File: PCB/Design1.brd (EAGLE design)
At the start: 70 x 42 mm, 34 parts, among them J1 FTDI_DEVICE, U1 ATMEGA2560AU

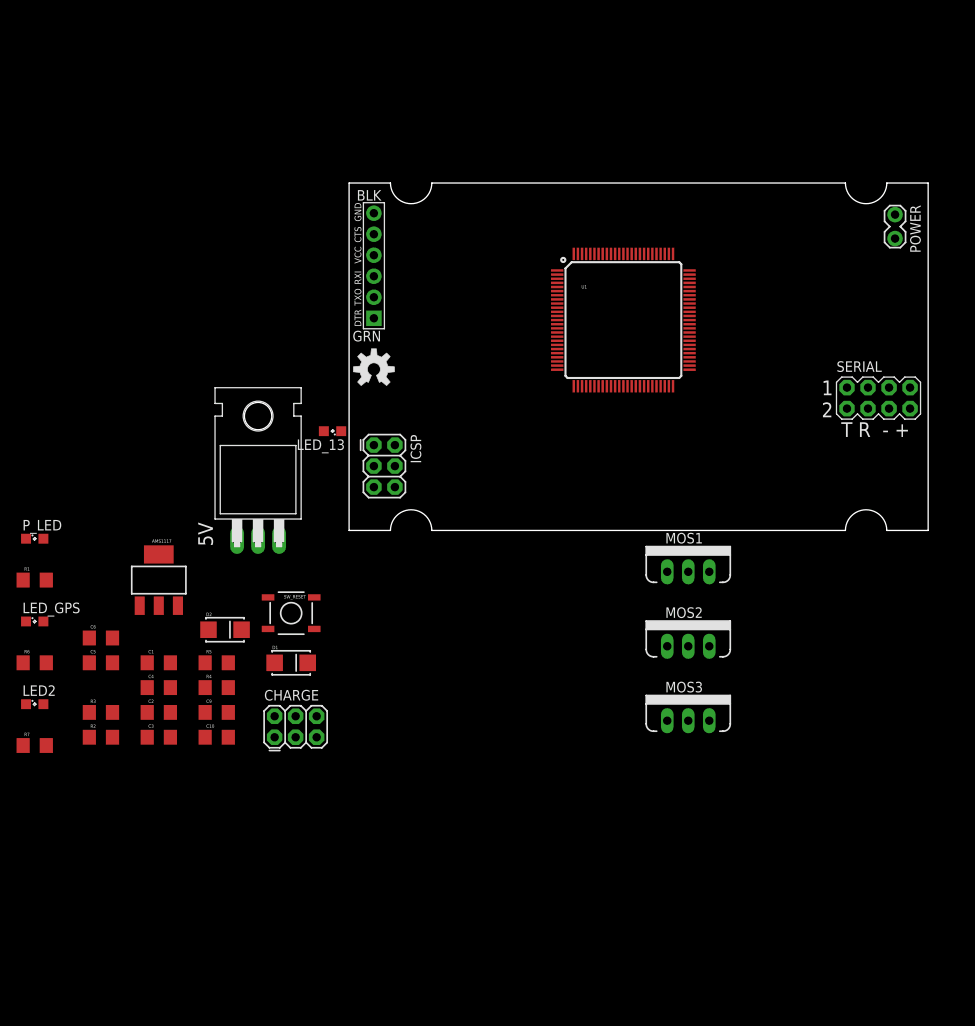
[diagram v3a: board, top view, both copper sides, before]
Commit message: Place mosfets
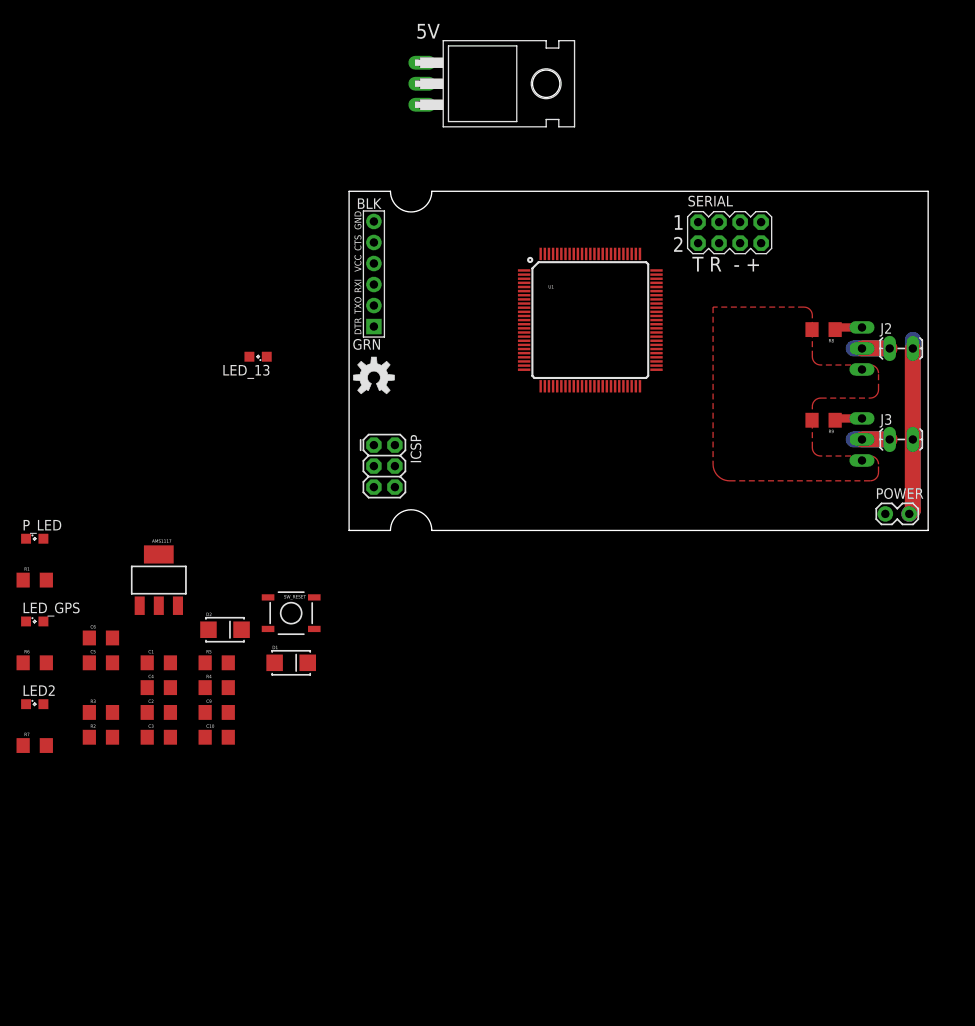
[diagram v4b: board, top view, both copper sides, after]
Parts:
- removed CHARGE: (no value), SparkFun-Connectors:2X3
- removed MOS3: (no value), SparkFun-DiscreteSemi:TO220V
- added J2, J3: (no value), SparkFun-Connectors:1X02_LOCK_LONGPADS
- added R8, R9: 10KΩ, SparkFun-Resistors:1206
- moved 5V 54.1 mm to (19.0, 54.0), turned to 270 degrees
- moved POWER 36.0 mm to (65.0, 2.00), turned to 0 degrees
- moved MOS1 34.2 mm to (62.0, 22.0), flipped to the bottom, turned to 270 degrees
- moved MOS2 32.6 mm to (62.0, 11.0), flipped to the bottom, turned to 270 degrees
- moved SERIAL 26.9 mm to (46.0, 36.0)
- moved LED_13 12.7 mm to (-11.0, 21.0)
- moved U1 4.00 mm to (29.2, 25.4)
- moved J1 1.00 mm to (3.00, 31.0)
- moved LOGO1 1.00 mm to (3.00, 18.5)
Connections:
- removed net CHARGE3: CHARGE.5
- removed net RAW: D2.A, POWER.2
- new net MOS1: J2.1, MOS1.2
- new net MOS2: J3.1, MOS2.2
- new net N$8: 5V.1, C1.1, C2.1, D2.C, R4.1
- net CHARGE1: now also MOS1.1, R8.1; no longer CHARGE.1
- net CHARGE2: now also MOS2.1, R9.1; no longer CHARGE.3
- net GND: now also R8.2, R9.2; no longer CHARGE.2, CHARGE.4, CHARGE.6, MOS3.3
- net VIN: now also D2.A, J2.2, J3.2, POWER.2; no longer 5V.1, C1.1, C2.1, D2.C, R4.1
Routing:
- net VIN: track 0.00 -> 41.4 mm
- net N$6: track 0.00 -> 4.00 mm
- net N$5: track 0.00 -> 4.00 mm
- net MOS2: track 0.00 -> 3.35 mm
- net MOS1: track 0.00 -> 3.35 mm
- net CHARGE1: track 0.00 -> 3.35 mm
- net CHARGE2: track 0.00 -> 3.33 mm
- added copper zone on layer 1, net GND
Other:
- board size 70 x 42 mm -> 70 x 41 mm

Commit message: switch to SMT 5v regulators
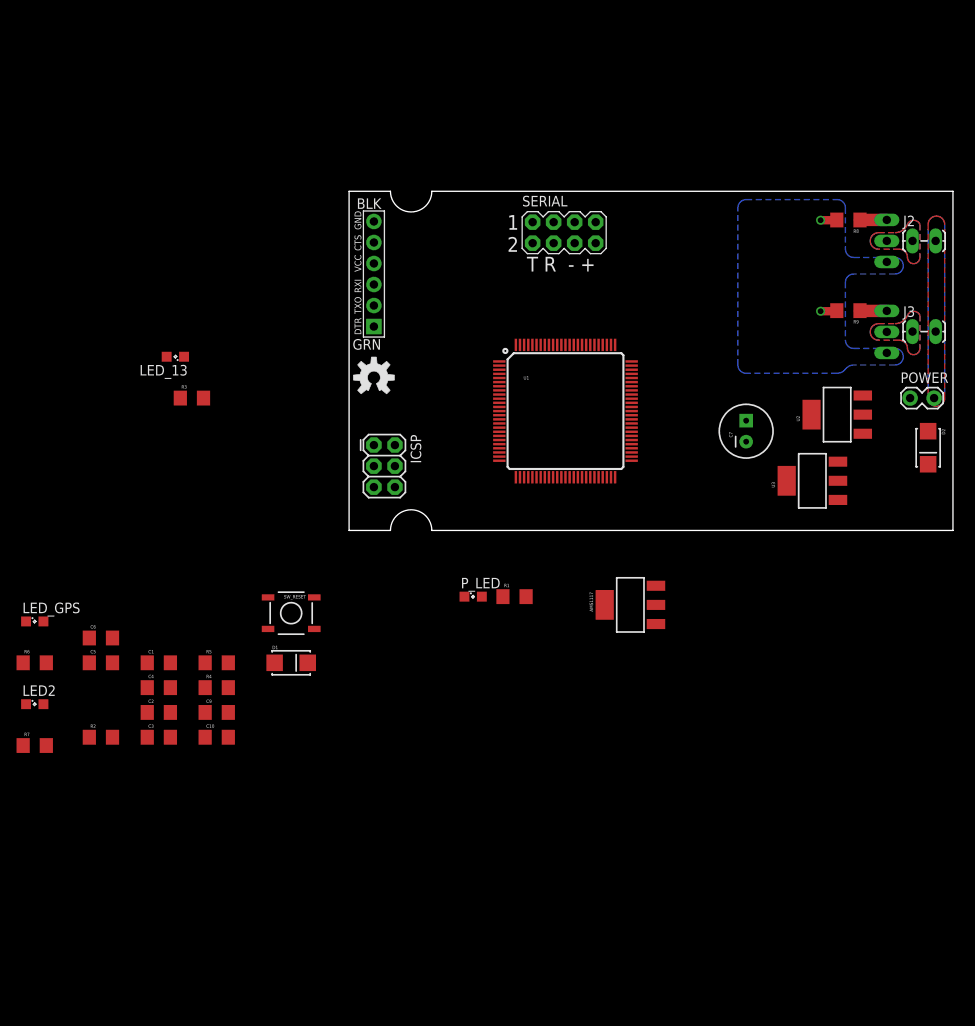
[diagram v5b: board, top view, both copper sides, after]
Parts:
- removed 5V: 7805, linear:TO220H
- added C7: 470uF, SparkFun-Capacitors:CPOL-RADIAL-100UF-25V
- added U2, U3: (no value), SparkFun-PowerIC:SOT223
- moved D2 87.8 mm to (70.0, 10.0), turned to 270 degrees
- moved R1 58.0 mm to (20.0, -8.00)
- moved AMS1117 57.1 mm to (34.0, -9.00), turned to 90 degrees
- moved P_LED 53.5 mm to (15.0, -8.00)
- moved R3 39.6 mm to (-19.0, 16.0)
- moved SERIAL 20.0 mm to (26.0, 36.0)
- moved POWER 14.3 mm to (68.0, 16.0)
- moved R8 13.6 mm to (60.4, 37.5)
- moved R9 13.6 mm to (60.4, 26.6)
- moved MOS1 13.3 mm to (65.0, 35.0)
- moved MOS2 13.3 mm to (65.0, 24.0)
- moved J3 13.3 mm to (68.2, 24.0)
- moved J2 13.3 mm to (68.2, 35.0)
- moved U1 11.4 mm to (26.2, 14.4)
- moved LED_13 10.0 mm to (-21.0, 21.0)
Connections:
- net 5V: now also C7.1, U2.2, U2.4, U3.2, U3.4; no longer 5V.3
- net GND: now also C7.2, U2.1, U3.1; no longer 5V.2
- net N$8: now also U2.3, U3.3; no longer 5V.1
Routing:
- net VIN: track 41.4 -> 0.00 mm
- net GND: track 0.00 -> 4.02 mm, vias 0 -> 2
- net N$6: track 4.00 -> 0.00 mm
- net N$5: track 4.00 -> 0.00 mm
- net MOS2: track 3.35 -> 0.00 mm
- net MOS1: track 3.35 -> 0.00 mm
- added copper zone on layer 16, net GND
- added copper zone on layer 1, net MOS1
- added copper zone on layer 16, net MOS1
- added copper zone on layer 1, net MOS2
- added copper zone on layer 16, net MOS2
- added copper zone on layer 1, net VIN
- added copper zone on layer 16, net VIN
- removed copper zone on layer 1, net GND
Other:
- board size 70 x 41 mm -> 73 x 41 mm

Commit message: meh
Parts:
- added R10: 1MΩ, SparkFun-Resistors:1206
- added Y1: 16MHZ, SparkFun-FreqCtrl:RESONATOR-SMD
- moved C1 96.1 mm to (71.0, 4.00), turned to 270 degrees
- moved C2 94.4 mm to (67.8, 4.00), turned to 270 degrees
- moved R4 85.0 mm to (61.0, 17.0), turned to 180 degrees
- moved C3 83.5 mm to (51.8, 12.2), turned to 90 degrees
- moved R5 78.3 mm to (55.0, 17.0), turned to 180 degrees
- moved C4 77.6 mm to (48.0, 12.2), turned to 90 degrees
- moved C10 60.2 mm to (40.0, -3.00), flipped to the bottom, turned to 180 degrees
- moved C9 58.0 mm to (40.0, -7.00), flipped to the bottom, turned to 180 degrees
- moved C5 33.4 mm to (-9.00, 10.0)
- moved C6 33.4 mm to (-9.00, 13.0)
- moved LED2 33.4 mm to (-17.0, 5.00)
- moved LED_GPS 33.4 mm to (-17.0, 15.0)
- moved R2 33.4 mm to (-9.00, 1.00)
- moved R6 33.4 mm to (-17.0, 10.0)
- moved R7 33.4 mm to (-17.0, 0.00)
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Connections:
- net N$8 renamed VIN_RECTIFIED
- new net XTAL1: R10.1, U1.34, Y1.3
- new net XTAL2: R10.2, U1.33, Y1.1
- net GND: now also Y1.2
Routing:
- net 5V: track 0.00 -> 33.7 mm
- net VIN_RECTIFIED: track 0.00 -> 27.1 mm
- net GND: track 4.02 -> 25.4 mm, vias 2 -> 5
- net VIN: track 0.00 -> 3.28 mm
- net VSENSE: track 0.00 -> 3.20 mm
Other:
- outline, holes or cut-outs redrawn

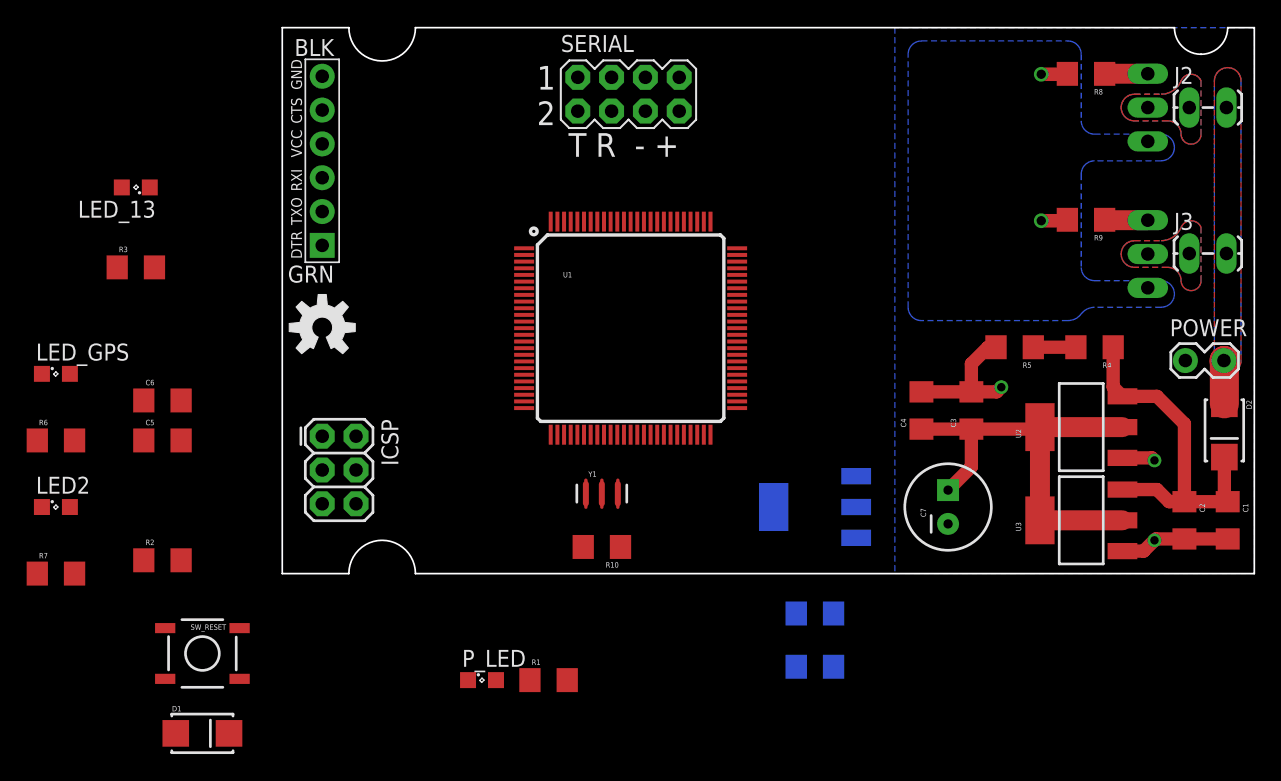
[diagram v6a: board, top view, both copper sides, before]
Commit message: Remove 3.3v; clean up Ground near MOSFETS #2
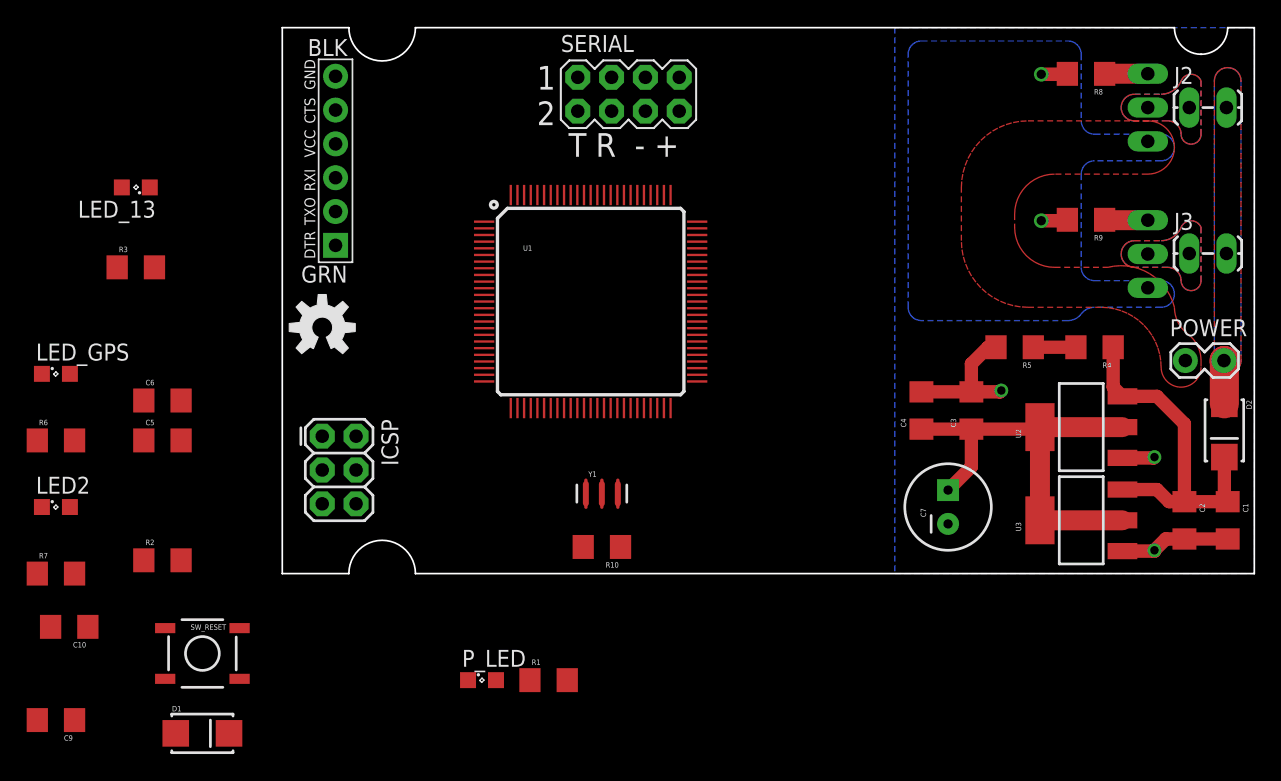
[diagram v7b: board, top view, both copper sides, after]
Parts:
- removed AMS1117: 3.3V, SparkFun-PowerIC:SOT223
- moved C9 57.1 mm to (-17.0, -11.0), flipped to the top
- moved C10 56.0 mm to (-16.0, -4.00), flipped to the top
- moved U1 3.61 mm to (23.2, 20.4)
- moved J1 1.00 mm to (4.00, 31.0)
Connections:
- removed net 3.3V: AMS1117.2, AMS1117.4, C10.1, C9.1, SERIAL.8
- net 5V: now also C10.1, C9.1, SERIAL.8; no longer AMS1117.3
- net GND: no longer AMS1117.1
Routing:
- added copper zone on layer 1, net GND

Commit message: Move componets to (hopefully) final location
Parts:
- moved D1 48.5 mm to (12.0, 33.0), turned to 180 degrees
- moved SW_RESET 44.2 mm to (19.0, 30.5), turned to 270 degrees
- moved R2 35.0 mm to (12.0, 29.0), turned to 180 degrees
- moved C5 31.8 mm to (19.0, 25.0), turned to 180 degrees
- moved P_LED 31.0 mm to (43.8, 3.50), turned to 90 degrees
- moved SERIAL 30.4 mm to (17.0, 7.00), turned to 90 degrees
- moved R1 29.7 mm to (44.0, 9.50), turned to 90 degrees
- moved C6 24.2 mm to (12.0, 25.0)
- moved U1 14.1 mm to (33.2, 30.4)
- moved R10 12.5 mm to (30.0, 13.0)
- moved Y1 12.5 mm to (30.0, 17.0)
- moved R7 12.0 mm to (-8.00, 8.00)
- moved LOGO1 11.7 mm to (7.00, 7.48)
- moved ICSP 11.0 mm to (8.32, 20.0), turned to 180 degrees
- moved R6 9.85 mm to (-8.00, 14.0)
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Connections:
- removed net VCC: D1.C, R2.2
- net 5V: now also D1.C, R2.2
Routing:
- net GND: track 25.3 -> 63.1 mm
- net RESET: track 0.00 -> 20.7 mm
- net 5V: track 33.7 -> 45.3 mm
- net DTR: track 0.00 -> 3.91 mm
- net N$2: track 0.00 -> 3.80 mm
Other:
- outline, holes or cut-outs redrawn
